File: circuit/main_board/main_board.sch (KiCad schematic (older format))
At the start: 19 parts

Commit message: Second revision
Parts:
- removed J? (x5): RJ45, symbol Connector:RJ45
- removed R? (x5): R, symbol Device:R
- removed U? (x6): POLOLU_A4988, symbol pololu_a4988:POLOLU_A4988
- added A? (x6): Pololu_Breakout_A4988, Module:Pololu_Breakout-16_15.2x20.3mm, symbol Driver_Motor:Pololu_Breakout_A4988
- added J? (x5): RJ45, Connector_RJ:RJ45_Wuerth_7499010121A_Horizontal, symbol Connector:RJ45
- added J?: Screw_Terminal_01x02, TerminalBlock:TerminalBlock_Altech_AK300-2_P5.00mm, symbol Connector:Screw_Terminal_01x02
- added R? (x5): R, Resistor_THT:R_Axial_DIN0309_L9.0mm_D3.2mm_P15.24mm_Horizontal, symbol Device:R
- J?: footprint (none) -> Connector_RJ:RJ45_Wuerth_7499010121A_Horizontal
- R?: footprint (none) -> Resistor_THT:R_Axial_DIN0309_L9.0mm_D3.2mm_P15.24mm_Horizontal
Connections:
- net +5V: now also J?.1, A?.13 (~RESET), A?.13 (~RESET), A?.13 (~RESET), A?.13 (~RESET), A?.13 (~RESET), A?.13 (~RESET), A?.14 (~SLEEP), A?.14 (~SLEEP), A?.14 (~SLEEP), A?.14 (~SLEEP), A?.14 (~SLEEP), A?.14 (~SLEEP), A?.2 (VDD), A?.2 (VDD), A?.2 (VDD), A?.2 (VDD), A?.2 (VDD), A?.2 (VDD), J?.1, J?.1, J?.1, J?.1, J?.1; no longer J?.8
- net DIR: now also A?.16 (DIR), A?.16 (DIR), A?.16 (DIR), A?.16 (DIR), A?.16 (DIR), A?.16 (DIR)
- net EN1: now also A?.9 (~ENABLE)
- net EN2: now also A?.9 (~ENABLE)
- net EN3: now also A?.9 (~ENABLE)
- net EN4: now also A?.9 (~ENABLE)
- net EN5: now also A?.9 (~ENABLE)
- net EN6: now also A?.9 (~ENABLE)
- net GND: now also A?.1 (GND), A?.1 (GND), A?.1 (GND), A?.1 (GND), A?.1 (GND), A?.1 (GND), A?.7 (GND), A?.7 (GND), A?.7 (GND), A?.7 (GND), A?.7 (GND), A?.7 (GND), J?.1 (Pin_1), R?.1, R?.1, R?.1, R?.1, R?.1
- net LIM1: now also J?.6, R?.2
- net LIM2: now also J?.6, R?.2
- net LIM3: now also J?.6, R?.2
- net LIM4: now also J?.6, R?.2
- net LIM5: now also J?.6, R?.2
- net LIM6: now also J?.6; no longer J?.3
- net MS1: now also A?.10 (MS1), A?.10 (MS1), A?.10 (MS1), A?.10 (MS1), A?.10 (MS1), A?.10 (MS1)
- net MS2: now also A?.11 (MS2), A?.11 (MS2), A?.11 (MS2), A?.11 (MS2), A?.11 (MS2), A?.11 (MS2)
- net MS3: now also A?.12 (MS3), A?.12 (MS3), A?.12 (MS3), A?.12 (MS3), A?.12 (MS3), A?.12 (MS3)
- net STEP: now also A?.15 (STEP), A?.15 (STEP), A?.15 (STEP), A?.15 (STEP), A?.15 (STEP), A?.15 (STEP)
- net VCC: now also A?.30 (VIN), A?.8 (VMOT), A?.8 (VMOT), A?.8 (VMOT), A?.8 (VMOT), A?.8 (VMOT), A?.8 (VMOT), J?.2 (Pin_2)
- net at J?.5: now also A?.3 (1B)
- net at J?.4: now also A?.4 (1A)
- net at J?.2: now also A?.6 (2B)
- new net: A?.3 (1B), J?.5 (x5)
- new net: A?.4 (1A), J?.4 (x5)
- new net: A?.5 (2A), J?.3 (x6)
- new net: A?.6 (2B), J?.2 (x5)
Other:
- note added: "VCC should be 8-10V"
- moved on the sheet: A?, J?

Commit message: Startet work on 1 layer pcb
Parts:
- removed R? (x5): R, Resistor_THT:R_Axial_DIN0309_L9.0mm_D3.2mm_P15.24mm_Horizontal, symbol Device:R
- added JI1, JI2, JI3, JI4, JI5, JI6: Conn_01x06, Connector_PinHeader_2.54mm:PinHeader_1x06_P2.54mm_Vertical, symbol Connector_Generic:Conn_01x06
- added JO2_1, JO2_2, JO2_3, JO2_4, JO2_5, JO2_6: Conn_01x02, Connector_PinHeader_2.54mm:PinHeader_1x02_P2.54mm_Vertical, symbol Connector_Generic:Conn_01x02
- added JO4_1, JO4_2, JO4_3, JO4_4, JO4_5, JO4_6: Conn_01x04, Connector_PinHeader_2.54mm:PinHeader_1x04_P2.54mm_Vertical, symbol Connector_Generic:Conn_01x04
- added R1, R2, R3, R4, R5: 2K2, Resistor_THT:R_Axial_DIN0309_L9.0mm_D3.2mm_P15.24mm_Horizontal, symbol Device:R
- R6: renamed from R?; value R -> 2K2
- gave numbers to parts that had none: 14
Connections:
- net +5V: now also J1.8, J2.8, J3.8, J4.8, J5.8, J6.8; no longer J1.1, J2.1, J3.1, J4.1, J5.1, J6.1
- net DIR: now also A7.9 (D6), JI1.2 (Pin_2), JI2.2 (Pin_2), JI3.2 (Pin_2), JI4.2 (Pin_2), JI5.2 (Pin_2), JI6.2 (Pin_2); no longer A1.16 (DIR), A2.16 (DIR), A3.16 (DIR), A4.16 (DIR), A5.16 (DIR), A6.16 (DIR), A7.5 (D2)
- net EN1: now also A7.12 (D9), JI1.1 (Pin_1); no longer A1.9 (~ENABLE), A7.10 (D7)
- net EN2: now also JI2.1 (Pin_1); no longer A2.9 (~ENABLE)
- net EN3: now also A7.10 (D7), JI3.1 (Pin_1); no longer A3.9 (~ENABLE), A7.12 (D9)
- net EN4: now also JI4.1 (Pin_1); no longer A4.9 (~ENABLE)
- net EN5: now also JI5.1 (Pin_1); no longer A5.9 (~ENABLE)
- net EN6: now also JI6.1 (Pin_1); no longer A6.9 (~ENABLE)
- net GND: now also R1.1, R2.1, R3.1, R4.1, R5.1
- net LIM1: now also A7.24 (A5), R4.2; no longer A7.21 (A2)
- net LIM2: now also A7.25 (A6), R5.2; no longer A7.22 (A3)
- net LIM3: now also A7.26 (A7), R6.2; no longer A7.23 (A4)
- net LIM4: now also A7.23 (A4), R3.2; no longer A7.24 (A5)
- net LIM5: now also A7.22 (A3), R2.2; no longer A7.25 (A6)
- net LIM6: now also A7.21 (A2), R1.2; no longer A7.26 (A7), R6.2
- net MS1: now also A7.5 (D2), JI1.6 (Pin_6), JI2.6 (Pin_6), JI3.6 (Pin_6), JI4.6 (Pin_6), JI5.6 (Pin_6), JI6.6 (Pin_6); no longer A1.10 (MS1), A2.10 (MS1), A3.10 (MS1), A4.10 (MS1), A5.10 (MS1), A6.10 (MS1), A7.7 (D4)
- net MS2: now also A7.6 (D3), JI1.5 (Pin_5), JI2.5 (Pin_5), JI3.5 (Pin_5), JI4.5 (Pin_5), JI5.5 (Pin_5), JI6.5 (Pin_5); no longer A1.11 (MS2), A2.11 (MS2), A3.11 (MS2), A4.11 (MS2), A5.11 (MS2), A6.11 (MS2), A7.8 (D5)
- net MS3: now also A7.7 (D4), JI1.4 (Pin_4), JI2.4 (Pin_4), JI3.4 (Pin_4), JI4.4 (Pin_4), JI5.4 (Pin_4), JI6.4 (Pin_4); no longer A1.12 (MS3), A2.12 (MS3), A3.12 (MS3), A4.12 (MS3), A5.12 (MS3), A6.12 (MS3), A7.9 (D6)
- net STEP: now also A7.8 (D5), JI1.3 (Pin_3), JI2.3 (Pin_3), JI3.3 (Pin_3), JI4.3 (Pin_3), JI5.3 (Pin_3), JI6.3 (Pin_3); no longer A1.15 (STEP), A2.15 (STEP), A3.15 (STEP), A4.15 (STEP), A5.15 (STEP), A6.15 (STEP), A7.6 (D3)
- net at A1.3 (1B): now also J1.7; no longer J1.5
- net at A1.4 (1A): now also J1.5; no longer J1.4
- net at A1.5 (2A): now also J1.1; no longer J1.3
- net at A2.3 (1B): now also J2.7; no longer J2.5
- net at A2.4 (1A): now also J2.5; no longer J2.4
- net at A2.5 (2A): now also J2.1; no longer J2.3
- net at A3.3 (1B): now also J3.7; no longer J3.5
- net at A3.4 (1A): now also J3.5; no longer J3.4
- net at A3.5 (2A): now also J3.1; no longer J3.3
- net at A4.3 (1B): now also J4.7; no longer J4.5
- net at A4.4 (1A): now also J4.5; no longer J4.4
- net at A4.5 (2A): now also J4.1; no longer J4.3
- net at A5.3 (1B): now also J5.7; no longer J5.5
- net at A5.4 (1A): now also J5.5; no longer J5.4
- net at A5.5 (2A): now also J5.1; no longer J5.3
- net at A6.3 (1B): now also J6.7; no longer J6.5
- net at A6.4 (1A): now also J6.5; no longer J6.4
- net at A6.5 (2A): now also J6.1; no longer J6.3
- new net: A1.10 (MS1), JO4_1.2 (Pin_2)
- new net: A1.11 (MS2), JO4_1.3 (Pin_3)
- new net: A1.12 (MS3), JO4_1.4 (Pin_4)
- new net: A1.15 (STEP), JO2_1.1 (Pin_1)
- new net: A1.16 (DIR), JO2_1.2 (Pin_2)
- new net: A1.9 (~ENABLE), JO4_1.1 (Pin_1)
- new net: A2.10 (MS1), JO4_2.2 (Pin_2)
- new net: A2.11 (MS2), JO4_2.3 (Pin_3)
- new net: A2.12 (MS3), JO4_2.4 (Pin_4)
- new net: A2.15 (STEP), JO2_2.1 (Pin_1)
- new net: A2.16 (DIR), JO2_2.2 (Pin_2)
- new net: A2.9 (~ENABLE), JO4_2.1 (Pin_1)
- new net: A3.10 (MS1), JO4_3.2 (Pin_2)
- new net: A3.11 (MS2), JO4_3.3 (Pin_3)
- new net: A3.12 (MS3), JO4_3.4 (Pin_4)
- new net: A3.15 (STEP), JO2_3.1 (Pin_1)
- new net: A3.16 (DIR), JO2_3.2 (Pin_2)
- new net: A3.9 (~ENABLE), JO4_3.1 (Pin_1)
- new net: A4.10 (MS1), JO4_4.2 (Pin_2)
- new net: A4.11 (MS2), JO4_4.3 (Pin_3)
- new net: A4.12 (MS3), JO4_4.4 (Pin_4)
- new net: A4.15 (STEP), JO2_4.1 (Pin_1)
- new net: A4.16 (DIR), JO2_4.2 (Pin_2)
- new net: A4.9 (~ENABLE), JO4_4.1 (Pin_1)
- new net: A5.10 (MS1), JO4_5.2 (Pin_2)
- new net: A5.11 (MS2), JO4_5.3 (Pin_3)
- new net: A5.12 (MS3), JO4_5.4 (Pin_4)
- new net: A5.15 (STEP), JO2_5.1 (Pin_1)
- new net: A5.16 (DIR), JO2_5.2 (Pin_2)
- new net: A5.9 (~ENABLE), JO4_5.1 (Pin_1)
- new net: A6.10 (MS1), JO4_6.2 (Pin_2)
- new net: A6.11 (MS2), JO4_6.3 (Pin_3)
- new net: A6.12 (MS3), JO4_6.4 (Pin_4)
- new net: A6.15 (STEP), JO2_6.1 (Pin_1)
- new net: A6.16 (DIR), JO2_6.2 (Pin_2)
- new net: A6.9 (~ENABLE), JO4_6.1 (Pin_1)
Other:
- moved on the sheet: J7

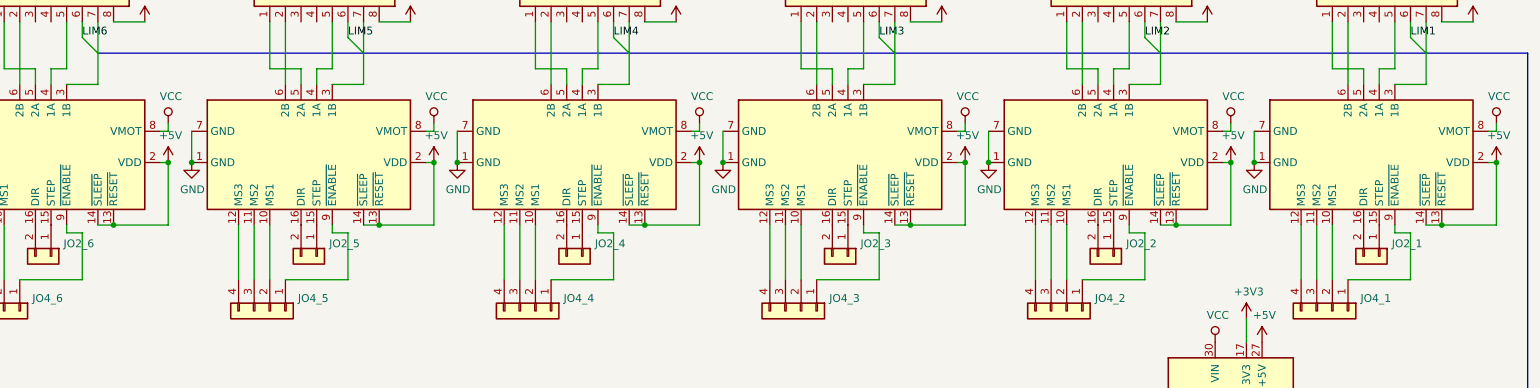
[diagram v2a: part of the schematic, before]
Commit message: Removed connection from sleep and reset to 5v
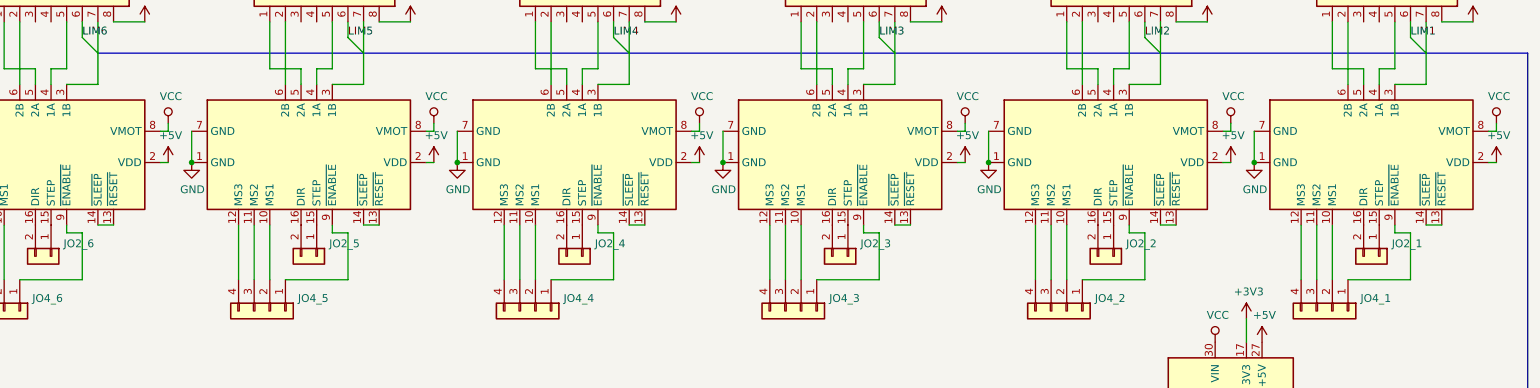
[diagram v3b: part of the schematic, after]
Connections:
- net +5V: no longer A1.13 (~RESET), A1.14 (~SLEEP), A2.13 (~RESET), A2.14 (~SLEEP), A3.13 (~RESET), A3.14 (~SLEEP), A4.13 (~RESET), A4.14 (~SLEEP), A5.13 (~RESET), A5.14 (~SLEEP), A6.13 (~RESET), A6.14 (~SLEEP)
- new net: A1.13 (~RESET), A1.14 (~SLEEP)
- new net: A2.13 (~RESET), A2.14 (~SLEEP)
- new net: A3.13 (~RESET), A3.14 (~SLEEP)
- new net: A4.13 (~RESET), A4.14 (~SLEEP)
- new net: A5.13 (~RESET), A5.14 (~SLEEP)
- new net: A6.13 (~RESET), A6.14 (~SLEEP)
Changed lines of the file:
@@
 Wire Wire Line
 	10450 3250 10550 3250
-Wire Wire Line
-	10550 3250 10900 3250
-Wire Wire Line
-	10900 3250 10900 2850
-Connection ~ 10550 3250
-Connection ~ 10900 2850
 $Comp
 L Driver_Motor:Pololu_Breakout_A4988 A2
@@
 Wire Wire Line
 	8750 3250 8850 3250
-Wire Wire Line
-	8850 3250 9200 3250
-Wire Wire Line
-	9200 3250 9200 2850
-Connection ~ 8850 3250
-Connection ~ 9200 2850
 $Comp
 L Driver_Motor:Pololu_Breakout_A4988 A3
@@
 Wire Wire Line
 	7050 3250 7150 3250
-Wire Wire Line
-	7150 3250 7500 3250
-Wire Wire Line
-	7500 3250 7500 2850
-Connection ~ 7150 3250
-Connection ~ 7500 2850
 $Comp
 L Driver_Motor:Pololu_Breakout_A4988 A4
@@
 Wire Wire Line
 	5350 3250 5450 3250
-Wire Wire Line
-	5450 3250 5800 3250
-Wire Wire Line
-	5800 3250 5800 2850
-Connection ~ 5450 3250
-Connection ~ 5800 2850
 $Comp
 L Driver_Motor:Pololu_Breakout_A4988 A5
@@
 Wire Wire Line
 	3650 3250 3750 3250
-Wire Wire Line
-	3750 3250 4100 3250
-Wire Wire Line
-	4100 3250 4100 2850
-Connection ~ 3750 3250
-Connection ~ 4100 2850
 $Comp
 L Driver_Motor:Pololu_Breakout_A4988 A6
@@
 Wire Wire Line
 	1950 3250 2050 3250
-Wire Wire Line
-	2050 3250 2400 3250
-Wire Wire Line
-	2400 3250 2400 2850
-Connection ~ 2050 3250
-Connection ~ 2400 2850
 $Comp
 L Connector:RJ45 J5
